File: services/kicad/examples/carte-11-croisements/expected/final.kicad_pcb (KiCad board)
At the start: 2 copper layers, 90 x 60 mm, 6 parts, among them J1 BUS_A, J2 BUS_B

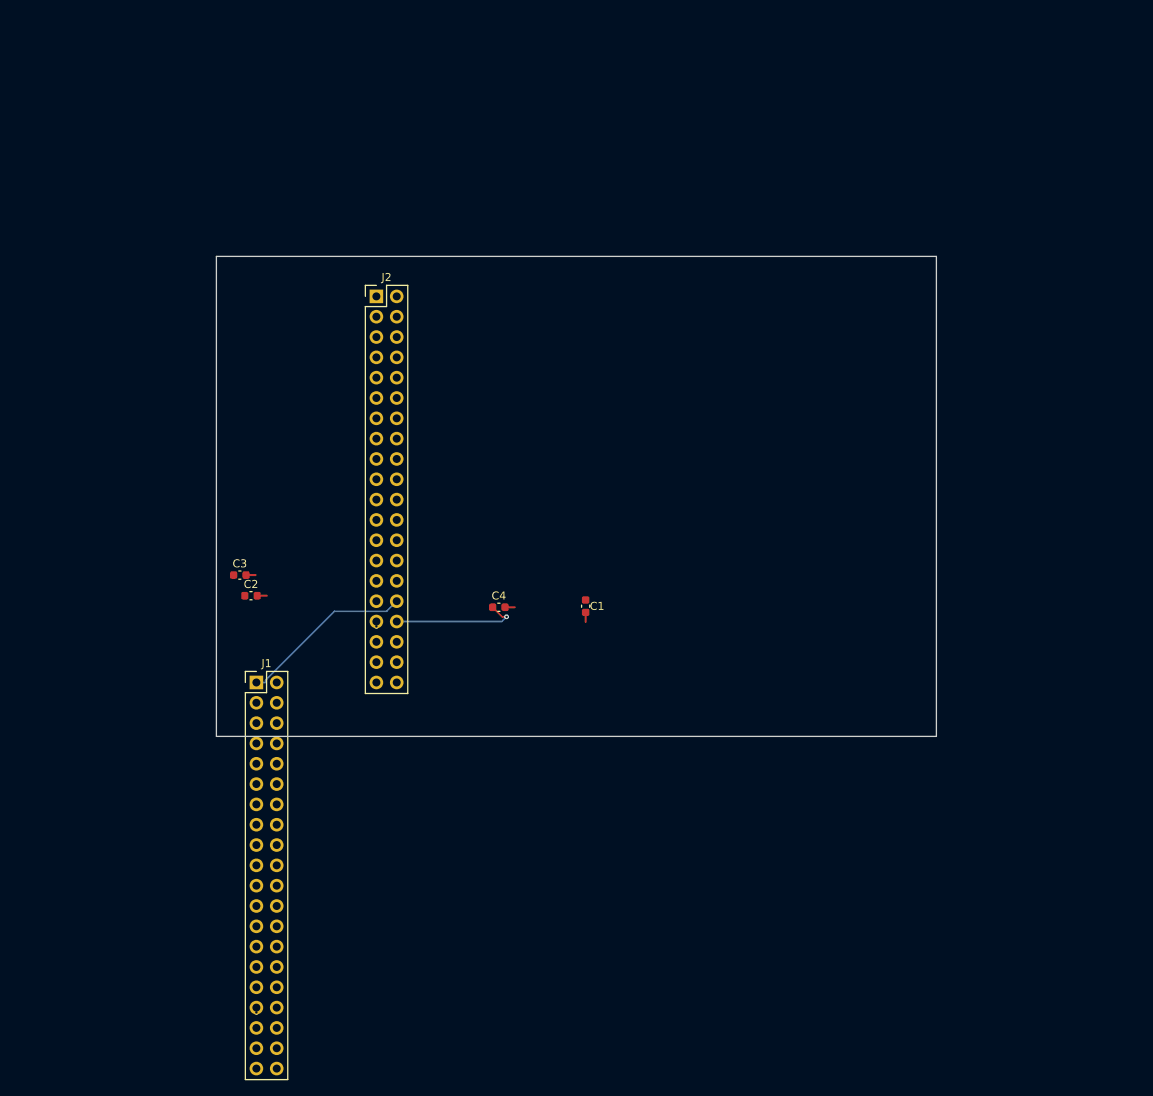
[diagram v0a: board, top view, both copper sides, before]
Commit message: fix(pcb): une carte livree n avait AUCUN CONTOUR, et sortait « 100 % routee »
DEUX CARTES ECHOUAIENT ; LEURS DEUX CAUSES SONT TROUVEES, ET AUCUNE N ETAIT LA
OU JE CHERCHAIS.

carte-11 : LE SCHEMA DEMANDAIT L IMPOSSIBLE

Livree a 3 % route et 42 erreurs depuis toujours. J ai interroge le routeur,
l escalade de couches, le nombre de tirages — six tirages perdus. La cause est
geometrique et la garde de placement la disait deja :

    reparation hors-carte : J1 (encombrement 51,1 mm) ne tient pas dans le contour

Un connecteur 2x20 vertical rend un encombrement de 49,1 mm, soit une marge
exigee de 51,1. Sur 60 mm de haut, la plage de positions valides etait NEGATIVE
(60 - 2x51,1 = -42) : aucune position n existait. `J1` sortait de 43,3 mm, et
Freerouting ne se figeait pas — IL N AVAIT RIEN A ROUTER.

Carte portee a 140 x 120 mm, la raison inscrite dans son schema. Resultat :

    3 % / 42 erreurs   ->   100 % / 0 erreur / DRC clean / 45 vias / 2 couches

⚠️ ET ELLE TIENT SUR DEUX COUCHES. Les 32 signaux croises — l objet meme de ce
cas de test — passent sans escalade. L escalade fonctionne (journal a l appui,
2 -> 4 couches), mais AUCUN de nos cas ne l exige. On ne vend pas une couche de
plus quand deux suffisent : elle coute plus cher a fabriquer.

carte-05 : LE CONTOUR ETAIT SUR LA MAUVAISE COUCHE

    edge_layer = 44  # Edge.Cuts     <- le code
    (25 "Edge.Cuts" user)            <- ce que KiCad 10 declare

44 etait le bon numero jusqu a KiCad 7. En KiCad 10 il designe une couche
INTERNE. Les quatre segments du contour etaient donc ecrits sur `In21.Cu`, que
ce board a DEUX couches ne declare meme pas :

    (gr_line (start 0 0) (end 70 0) (layer "In21.Cu"))

La carte n avait AUCUN CONTOUR. Ses cinq erreurs, en un seul defaut :

    invalid_outline          1    il n y a rien sur Edge.Cuts
    item_on_disabled_layer   4    les quatre segments, orphelins

⚠️ ET ELLE SORTAIT « 100 % ROUTEE ». Le routeur travaille sur les pastilles, pas
sur la forme du board : l absence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
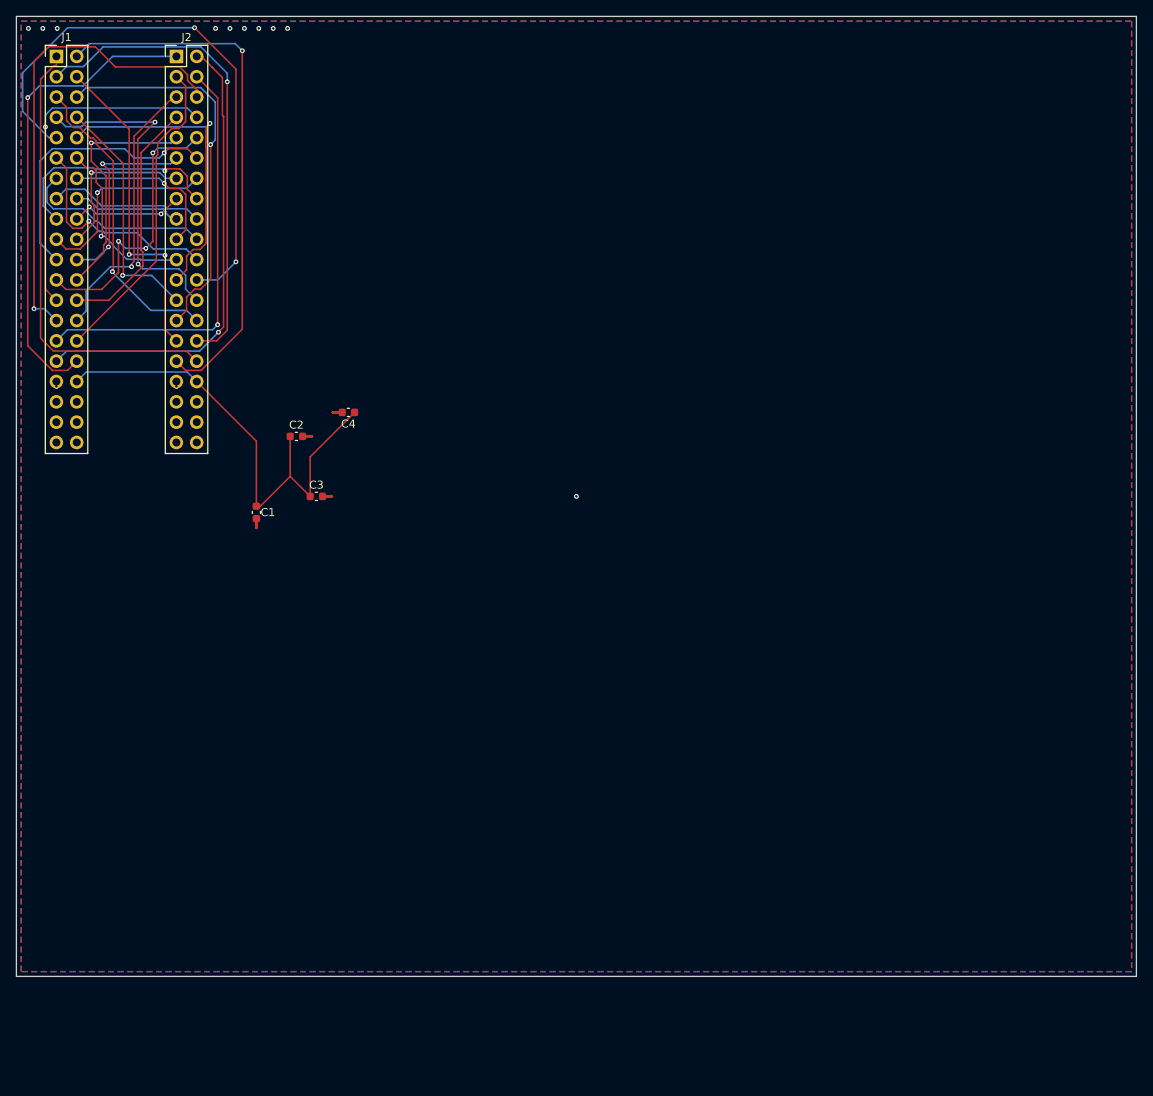
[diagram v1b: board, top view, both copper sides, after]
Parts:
- moved J1 82.2 mm to (83.5, 50.0)
- moved C1 42.8 mm to (108.5, 107.0)
- moved J2 39.1 mm to (98.5, 50.0)
- moved C4 30.8 mm to (120.0, 94.5), turned to 180 degrees
- moved C2 20.7 mm to (113.5, 97.5)
- moved C3 13.7 mm to (116.0, 105.0)
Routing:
- net X09: track 0.00 -> 71.5 mm, vias 0 -> 2
- net X02: track 0.00 -> 67.4 mm, vias 0 -> 1
- net X03: track 0.00 -> 60.8 mm, vias 0 -> 1
- net X32: track 0.00 -> 59.6 mm, vias 0 -> 1
- net X27: track 0.00 -> 59.0 mm, vias 0 -> 1
- net X31: track 0.00 -> 58.4 mm, vias 0 -> 1
- net X29: track 0.00 -> 53.1 mm, vias 0 -> 1
- net X06: track 0.00 -> 48.3 mm, vias 0 -> 1
- net +3V3: track 16.2 -> 61.8 mm, vias 1 -> 0
- net X25: track 0.00 -> 43.5 mm, vias 0 -> 1
- net X07: track 0.00 -> 41.9 mm, vias 0 -> 2
- net X04: track 0.00 -> 40.7 mm, vias 0 -> 2
- net X30: track 0.00 -> 39.6 mm
- net X10: track 0.00 -> 39.2 mm, vias 0 -> 1
- net X05: track 0.00 -> 38.6 mm, vias 0 -> 1
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- added copper zone on B.Cu, net GND
- added copper zone on F.Cu, net GND
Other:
- board size 90 x 60 mm -> 140 x 120 mm

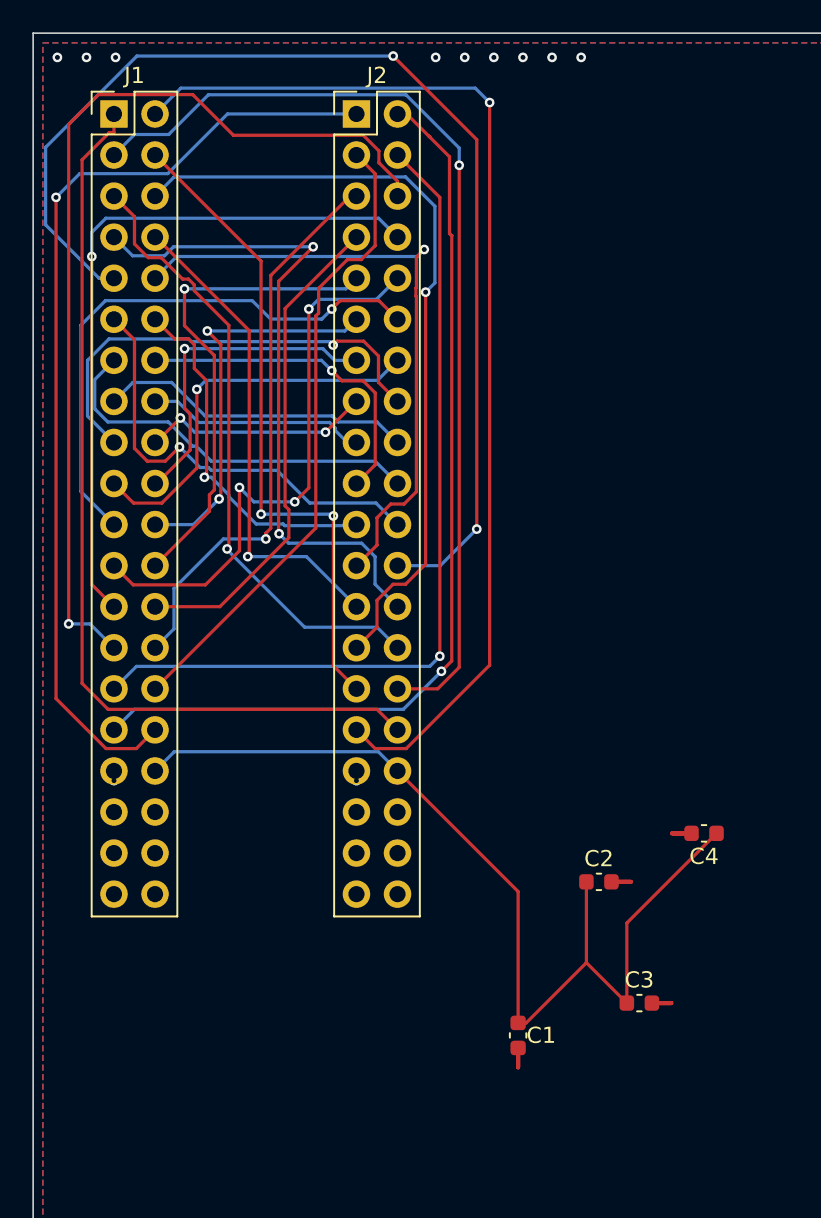
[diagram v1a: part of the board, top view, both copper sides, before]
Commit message: test(examples): carte-10 et carte-11 -- placements pro geles, routes a 100 %, 0 erreur, 4 couches
carte-10 : placement revalide avec la regle « une capa par broche dans le
halo » (decouplage median 4,1 mm), route a 100 % au 2e tirage (175 s).
carte-11 : 100 % au palier 4 couches. DRC local kicad-cli : 0 erreur,
0 non connecte sur les deux boards.

Co-Authored-By: Claude Fable 5.1 <noreply@anthropic.com>
Claude-Session: https://claude.ai/code/session_01TnMqm4La2CxQHHB5K8aSSV
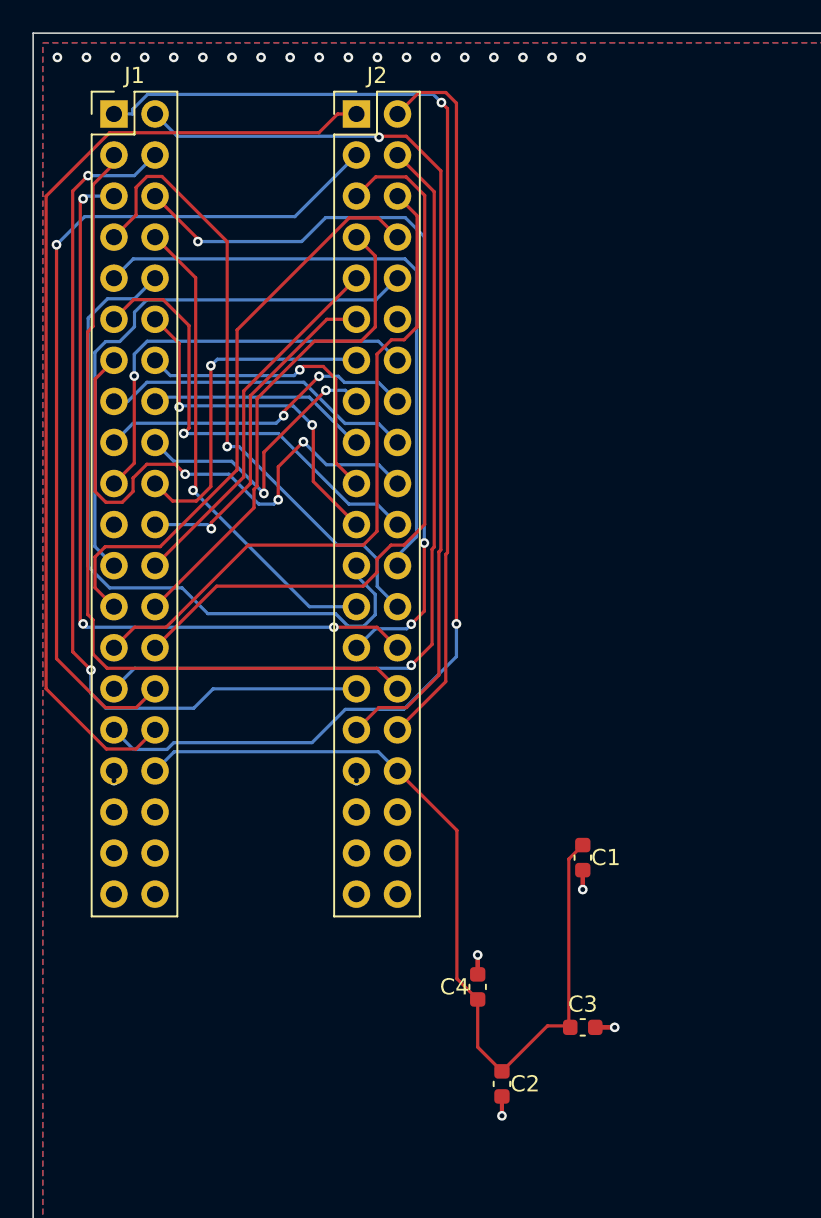
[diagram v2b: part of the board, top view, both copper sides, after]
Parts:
- moved C4 16.9 mm to (106.0, 104.0), turned to 90 degrees
- moved C2 13.9 mm to (107.5, 110.0), turned to -90 degrees
- moved C1 11.7 mm to (112.5, 96.0)
- moved C3 3.81 mm to (112.5, 106.5)
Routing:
- net X09: track 71.5 -> 38.3 mm, vias 2 -> 0
- net X27: track 59.0 -> 42.0 mm, vias 1 -> 0
- net X30: track 39.6 -> 54.3 mm, vias 0 -> 1
- net X04: track 40.7 -> 54.9 mm
- net X21: track 34.8 -> 23.8 mm, vias 1 -> 0
- net X28: track 34.9 -> 45.9 mm, vias 1 -> 0
- net X02: track 67.4 -> 56.9 mm
- net X05: track 38.6 -> 48.5 mm, vias 1 -> 3
- net X13: track 24.1 -> 33.9 mm, vias 0 -> 3
- net X03: track 60.8 -> 51.4 mm, vias 1 -> 0
- net X17: track 28.2 -> 20.0 mm, vias 1 -> 2
- net +3V3: track 61.8 -> 54.2 mm
- net X24: track 30.3 -> 22.9 mm, vias 1 -> 0
- net X25: track 43.5 -> 36.5 mm, vias 1 -> 0
- net X01: track 56.9 -> 61.4 mm, vias 0 -> 1
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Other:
- copper layers 2 -> 4
